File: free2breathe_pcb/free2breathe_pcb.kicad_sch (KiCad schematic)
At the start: 96 parts, among them J1 USB4110-GF-A_REVB, J2 LED_Connector, J3 Alarm_Connector, Q1 AO3401A, Q2 DMN3404L, SW1 Power_Switch, U1 IP5328, U2 MCP6044-E/P, U3 MCP6044-E/P, U4 SO2 Sensor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

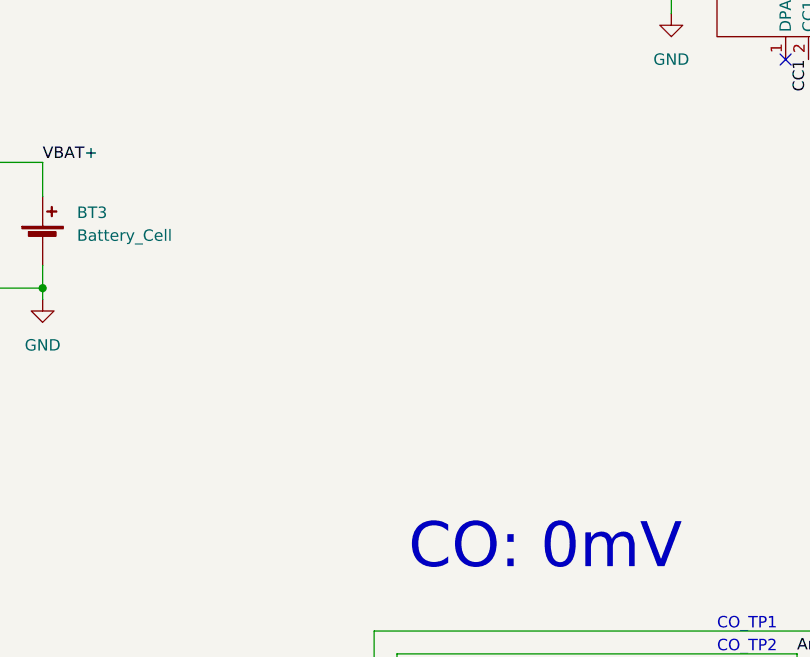
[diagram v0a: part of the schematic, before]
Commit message: initial arrangement for new layout, add mounting holes
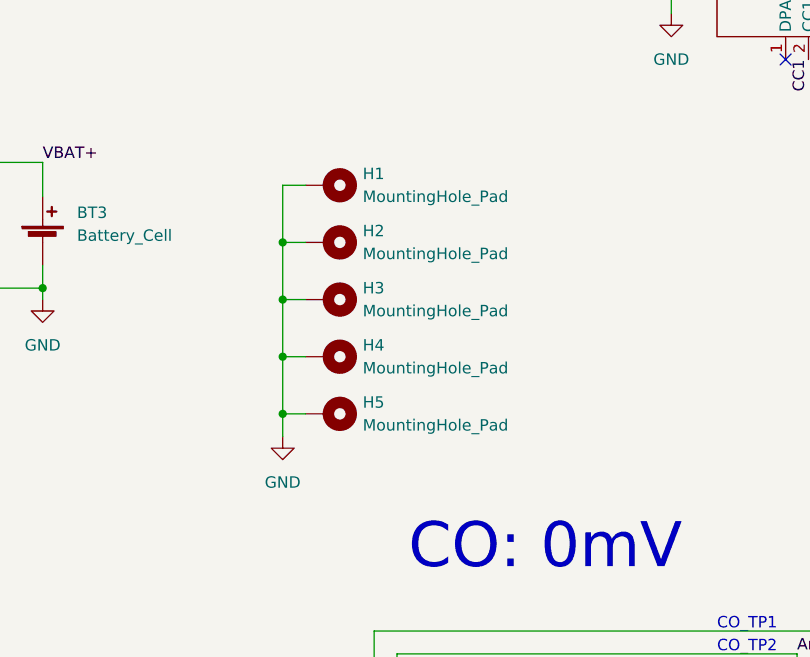
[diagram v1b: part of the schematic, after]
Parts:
- added H1, H2, H3, H4, H5: MountingHole_Pad, MountingHole:MountingHole_3.2mm_M3, symbol Mechanical:MountingHole_Pad
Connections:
- net GND: now also H1.1, H2.1, H3.1, H4.1, H5.1

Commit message: further refinement
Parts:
- J2: footprint Connector_JST:JST_PH_B3B-PH-K_1x03_P2.00mm_Vertical -> Connector_JST:JST_PH_S3B-PH-K_1x03_P2.00mm_Horizontal
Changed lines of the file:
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@@
       (effects (font (size 1.27 1.27)) (justify left))
     )
-    (property "Footprint" "Connector_JST:JST_PH_B3B-PH-K_1x03_P2.00mm_Vertical" (id 2) (at 398.78 88.9 0)
+    (property "Footprint" "Connector_JST:JST_PH_S3B-PH-K_1x03_P2.00mm_Horizontal" (id 2) (at 398.78 88.9 0)
       (effects (font (size 1.27 1.27)) hide)
     )
@@
     )
     (path "/c4414011-bc6e-427d-914d-4b02080af175"
-      (reference "J2") (unit 1) (value "LED_Connector") (footprint "Connector_JST:JST_PH_B3B-PH-K_1x03_P2.00mm_Vertical")
+      (reference "J2") (unit 1) (value "LED_Connector") (footprint "Connector_JST:JST_PH_S3B-PH-K_1x03_P2.00mm_Horizontal")
     )
     (path "/4bd3da1a-b4fb-485a-b13c-20d04d4b9acb"

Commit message: placed components, changed power LEDs
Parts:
- D5, D6, D7, D8: footprint LED_THT:LED_D3.0mm -> LED_SMD:LED_0603_1608Metric
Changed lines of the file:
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@@
     (property "Reference" "D5" (id 0) (at 203.2 118.11 0))
     (property "Value" "LED" (id 1) (at 207.01 121.92 0))
-    (property "Footprint" "LED_THT:LED_D3.0mm" (id 2) (at 203.2 120.65 0)
+    (property "Footprint" "LED_SMD:LED_0603_1608Metric" (id 2) (at 203.2 120.65 0)
       (effects (font (size 1.27 1.27)) hide)
     )
@@
     (property "Reference" "D8" (id 0) (at 193.04 135.89 0))
     (property "Value" "LED" (id 1) (at 196.85 134.62 0))
-    (property "Footprint" "LED_THT:LED_D3.0mm" (id 2) (at 193.04 133.35 0)
+    (property "Footprint" "LED_SMD:LED_0603_1608Metric" (id 2) (at 193.04 133.35 0)
       (effects (font (size 1.27 1.27)) hide)
     )
@@
     (property "Reference" "D7" (id 0) (at 193.04 127 0))
     (property "Value" "LED" (id 1) (at 196.85 130.81 0))
-    (property "Footprint" "LED_THT:LED_D3.0mm" (id 2) (at 193.04 129.54 0)
+    (property "Footprint" "LED_SMD:LED_0603_1608Metric" (id 2) (at 193.04 129.54 0)
       (effects (font (size 1.27 1.27)) hide)
     )
@@
     (property "Reference" "D6" (id 0) (at 200.66 123.19 0))
     (property "Value" "LED" (id 1) (at 203.2 127 0))
-    (property "Footprint" "LED_THT:LED_D3.0mm" (id 2) (at 203.2 124.46 0)
+    (property "Footprint" "LED_SMD:LED_0603_1608Metric" (id 2) (at 203.2 124.46 0)
       (effects (font (size 1.27 1.27)) hide)
     )
@@
     )
     (path "/0299984f-df78-48cc-bdc6-090d3e9cd159"
-      (reference "D5") (unit 1) (value "LED") (footprint "LED_THT:LED_D3.0mm")
+      (reference "D5") (unit 1) (value "LED") (footprint "LED_SMD:LED_0603_1608Metric")
     )
     (path "/b01b1188-32bd-4fd4-b4d9-a13c45d1c9c1"
-      (reference "D6") (unit 1) (value "LED") (footprint "LED_THT:LED_D3.0mm")
+      (reference "D6") (unit 1) (value "LED") (footprint "LED_SMD:LED_0603_1608Metric")
     )
     (path "/5d679726-a4e8-43e7-be42-4533ed656c2e"
-      (reference "D7") (unit 1) (value "LED") (footprint "LED_THT:LED_D3.0mm")
+      (reference "D7") (unit 1) (value "LED") (footprint "LED_SMD:LED_0603_1608Metric")
     )
     (path "/04248967-0a57-4abc-9e67-35cfb5f78fd9"
-      (reference "D8") (unit 1) (value "LED") (footprint "LED_THT:LED_D3.0mm")
+      (reference "D8") (unit 1) (value "LED") (footprint "LED_SMD:LED_0603_1608Metric")
     )
     (path "/3e058933-7aac-40cd-b441-79629738d0a3"

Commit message: more routing
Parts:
- H1, H2, H3, H4, H5: footprint MountingHole:MountingHole_3.2mm_M3 -> MountingHole:MountingHole_3.2mm_M3_Pad_Via
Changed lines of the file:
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@@
       (effects (font (size 1.27 1.27)) (justify left))
     )
-    (property "Footprint" "MountingHole:MountingHole_3.2mm_M3" (id 2) (at 105.41 146.05 0)
+    (property "Footprint" "MountingHole:MountingHole_3.2mm_M3_Pad_Via" (id 2) (at 105.41 146.05 0)
       (effects (font (size 1.27 1.27)) hide)
     )
@@
       (effects (font (size 1.27 1.27)) (justify left))
     )
-    (property "Footprint" "MountingHole:MountingHole_3.2mm_M3" (id 2) (at 105.41 139.7 0)
+    (property "Footprint" "MountingHole:MountingHole_3.2mm_M3_Pad_Via" (id 2) (at 105.41 139.7 0)
       (effects (font (size 1.27 1.27)) hide)
     )
@@
       (effects (font (size 1.27 1.27)) (justify left))
     )
-    (property "Footprint" "MountingHole:MountingHole_3.2mm_M3" (id 2) (at 105.41 152.4 0)
+    (property "Footprint" "MountingHole:MountingHole_3.2mm_M3_Pad_Via" (id 2) (at 105.41 152.4 0)
       (effects (font (size 1.27 1.27)) hide)
     )
@@
       (effects (font (size 1.27 1.27)) (justify left))
     )
-    (property "Footprint" "MountingHole:MountingHole_3.2mm_M3" (id 2) (at 105.41 165.1 0)
+    (property "Footprint" "MountingHole:MountingHole_3.2mm_M3_Pad_Via" (id 2) (at 105.41 165.1 0)
       (effects (font (size 1.27 1.27)) hide)
     )
@@
       (effects (font (size 1.27 1.27)) (justify left))
     )
-    (property "Footprint" "MountingHole:MountingHole_3.2mm_M3" (id 2) (at 105.41 158.75 0)
+    (property "Footprint" "MountingHole:MountingHole_3.2mm_M3_Pad_Via" (id 2) (at 105.41 158.75 0)
       (effects (font (size 1.27 1.27)) hide)
     )
@@
     )
     (path "/3e058933-7aac-40cd-b441-79629738d0a3"
-      (reference "H1") (unit 1) (value "MountingHole_Pad") (footprint "MountingHole:MountingHole_3.2mm_M3")
+      (reference "H1") (unit 1) (value "MountingHole_Pad") (footprint "MountingHole:MountingHole_3.2mm_M3_Pad_Via")
     )
     (path "/3ae0b7cc-c4c5-42a0-ba58-20994b18ddcb"
-      (reference "H2") (unit 1) (value "MountingHole_Pad") (footprint "MountingHole:MountingHole_3.2mm_M3")
+      (reference "H2") (unit 1) (value "MountingHole_Pad") (footprint "MountingHole:MountingHole_3.2mm_M3_Pad_Via")
     )
     (path "/44a4c3b3-90cd-4ca6-b7f3-8c329523b9c4"
-      (reference "H3") (unit 1) (value "MountingHole_Pad") (footprint "MountingHole:MountingHole_3.2mm_M3")
+      (reference "H3") (unit 1) (value "MountingHole_Pad") (footprint "MountingHole:MountingHole_3.2mm_M3_Pad_Via")
     )
     (path "/82e9b2e9-432f-44f2-956a-61a2e063503a"
-      (reference "H4") (unit 1) (value "MountingHole_Pad") (footprint "MountingHole:MountingHole_3.2mm_M3")
+      (reference "H4") (unit 1) (value "MountingHole_Pad") (footprint "MountingHole:MountingHole_3.2mm_M3_Pad_Via")
     )
     (path "/54570a55-2fea-47e6-9d91-f42ccc350ea4"
-      (reference "H5") (unit 1) (value "MountingHole_Pad") (footprint "MountingHole:MountingHole_3.2mm_M3")
+      (reference "H5") (unit 1) (value "MountingHole_Pad") (footprint "MountingHole:MountingHole_3.2mm_M3_Pad_Via")
     )
     (path "/da0efc7a-01ab-44ff-bf6d-4e1e4b0cafb5"

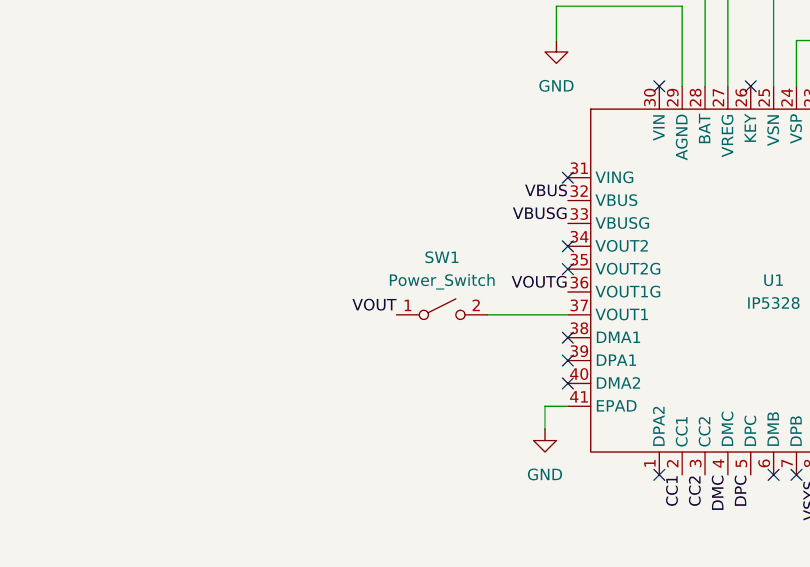
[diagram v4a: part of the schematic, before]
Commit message: add 3d models
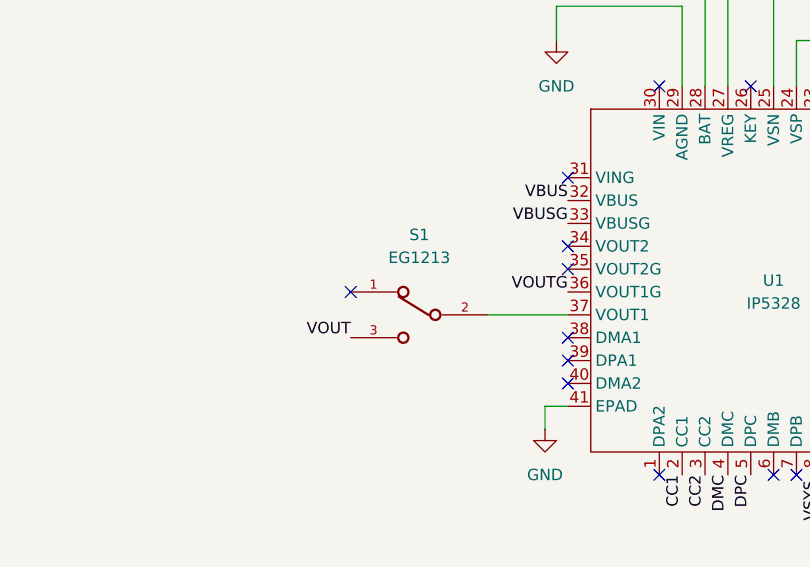
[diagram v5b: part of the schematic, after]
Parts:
- removed SW1: Power_Switch, switch:switch_pad, symbol Switch:SW_SPST
- added S1: EG1213, components:SW_EG1213, symbol EG1213:EG1213
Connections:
- net VOUT: now also S1.3
- net at U1.37 (VOUT1): now also S1.2
- no-connect marks 27 -> 28
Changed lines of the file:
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@@
   (no_connect (at 69.85 53.34))
   (no_connect (at 307.34 85.09))
+  (no_connect (at 121.92 105.41))
   (no_connect (at 171.45 125.73))
   (no_connect (at 34.29 58.42))
@@
     (effects (font (size 1.27 1.27)) (justify right bottom))
   )
-  (label "VOUT" (at 127 107.95 180)
+  (label "VOUT" (at 121.92 110.49 180)
     (effects (font (size 1.27 1.27)) (justify right bottom))
   )
@@
     (pin "2")
   )
+  (symbol (lib_id "EG1213:EG1213") (at 129.54 107.95 0) (unit 1)
+    (in_bom yes) (on_board yes) (fields_autoplaced)
+    (property "Reference" "S1" (id 0) (at 129.54 99.06 0))
+    (property "Value" "EG1213" (id 1) (at 129.54 101.6 0))
+    (property "Footprint" "components:SW_EG1213" (id 2) (at 129.54 107.95 0)
+      (effects (font (size 1.27 1.27)) (justify bottom) hide)
+    )
+    (property "Datasheet" "" (id 3) (at 129.54 107.95 0)
+      (effects (font (size 1.27 1.27)) hide)
+    )
+    (property "MANUFACTURER" "E-Switch" (id 4) (at 129.54 107.95 0)
+      (effects (font (size 1.27 1.27)) (justify bottom) hide)
+    )
+    (pin "1")
+    (pin "2")
+    (pin "3")
+  )
   (symbol (lib_id "power:GND") (at 92.71 309.88 0) (unit 1)
     (in_bom yes) (on_board yes) (fields_autoplaced)
@@
     (pin "2")
   )
-  (symbol (lib_id "Switch:SW_SPST") (at 132.08 107.95 0) (unit 1)
-    (in_bom yes) (on_board yes) (fields_autoplaced)
-    (property "Reference" "SW1" (id 0) (at 132.08 101.6 0))
-    (property "Value" "Power_Switch" (id 1) (at 132.08 104.14 0))
-    (property "Footprint" "switch:switch_pad" (id 2) (at 132.08 107.95 0)
-      (effects (font (size 1.27 1.27)) hide)
-    )
-    (property "Datasheet" "~" (id 3) (at 132.08 107.95 0)
-      (effects (font (size 1.27 1.27)) hide)
-    )
-    (pin "1")
-    (pin "2")
-  )
   (symbol (lib_id "Device:C") (at 212.09 81.28 0) (unit 1)
     (in_bom yes) (on_board yes)
@@
       (reference "R35") (unit 1) (value "10") (footprint "Resistor_SMD:R_0603_1608Metric")
     )
-    (path "/be04bd1f-0a32-47c6-ac53-a5332a5382ed"
-      (reference "SW1") (unit 1) (value "Power_Switch") (footprint "switch:switch_pad")
+    (path "/64b42584-270d-428b-a561-2aaf0f562d08"
+      (reference "S1") (unit 1) (value "EG1213") (footprint "components:SW_EG1213")
     )
     (path "/c9dcc37a-27d4-444a-93cb-b4b7d47a7bbd"

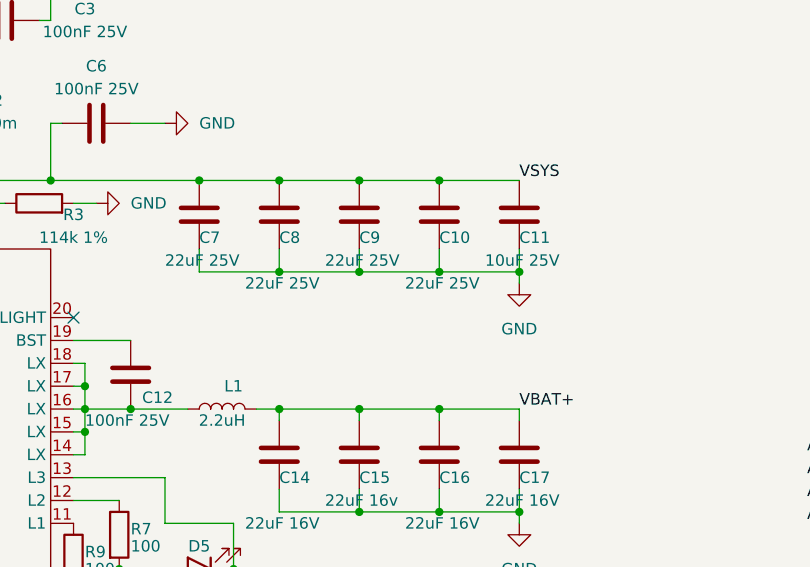
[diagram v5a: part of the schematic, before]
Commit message: update step file to include standard components
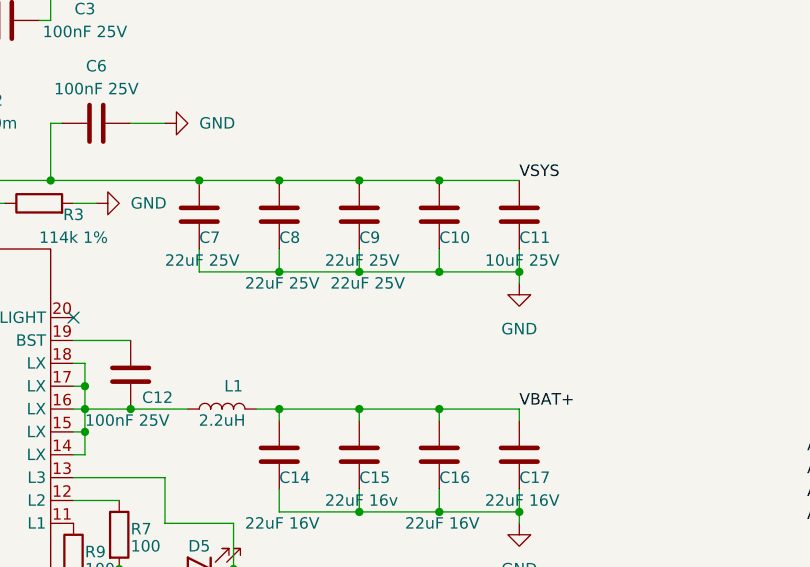
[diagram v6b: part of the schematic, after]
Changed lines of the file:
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@@
     )
     (property "Value" "22uF 25V" (id 1) (at 226.06 88.9 0)
-      (effects (font (size 1.27 1.27)) (justify left))
+      (effects (font (size 1.27 1.27)) (justify right))
     )
     (property "Footprint" "Capacitor_SMD:C_0603_1608Metric" (id 2) (at 230.8352 85.09 0)

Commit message: update components and todo, swap current-sense resistor to 0805
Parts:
- R2: footprint Resistor_SMD:R_0603_1608Metric -> Resistor_SMD:R_0805_2012Metric
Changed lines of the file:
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@@
   (no_connect (at 146.05 110.49))
   (no_connect (at 281.94 90.17))
+  (no_connect (at 166.37 82.55))
   (no_connect (at 281.94 87.63))
   (no_connect (at 146.05 92.71))
   (no_connect (at 146.05 115.57))
-  (no_connect (at 166.37 82.55))
   (no_connect (at 146.05 102.87))
   (no_connect (at 307.34 92.71))
@@
       (effects (font (size 1.27 1.27)) (justify left))
     )
-    (property "Footprint" "Resistor_SMD:R_0603_1608Metric" (id 2) (at 174.752 69.85 90)
+    (property "Footprint" "Resistor_SMD:R_0805_2012Metric" (id 2) (at 174.752 69.85 90)
       (effects (font (size 1.27 1.27)) hide)
     )
@@
     )
     (path "/aac64d76-0462-479d-882d-a1e685ec1bb8"
-      (reference "R2") (unit 1) (value "10m") (footprint "Resistor_SMD:R_0603_1608Metric")
+      (reference "R2") (unit 1) (value "10m") (footprint "Resistor_SMD:R_0805_2012Metric")
     )
     (path "/15f99abf-d997-4083-af3a-6835a9c72472"

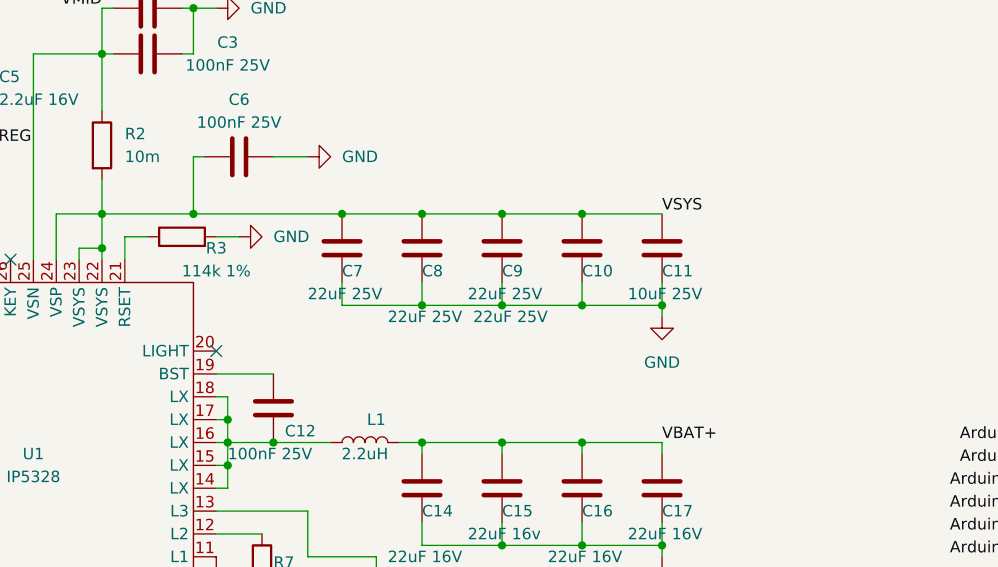
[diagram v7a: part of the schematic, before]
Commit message: add BOM, update board with component replacements
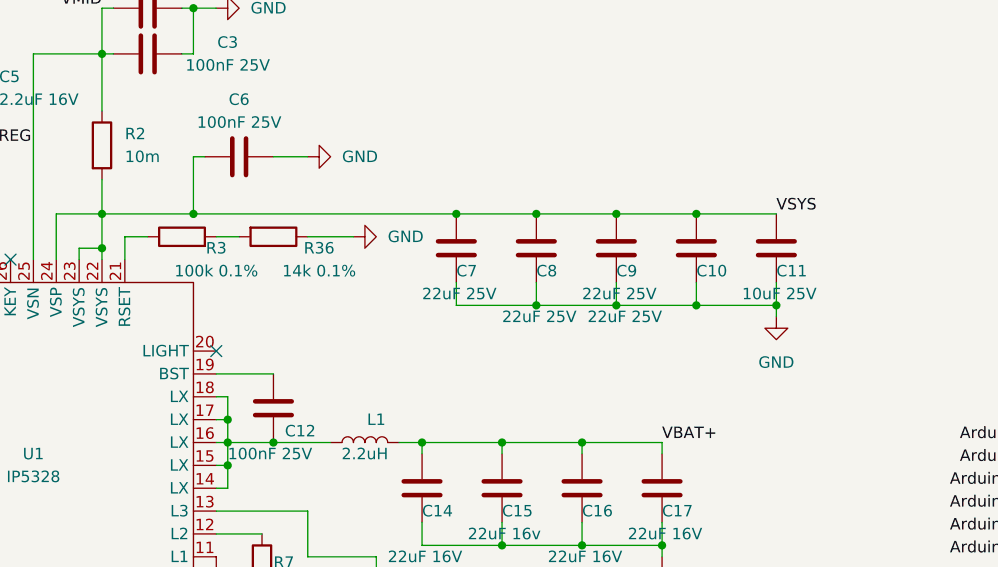
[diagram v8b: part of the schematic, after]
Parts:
- added R36: 14k 0.1%, Resistor_SMD:R_0603_1608Metric, symbol Device:R
- C10, C2, C7, C8, C9: footprint Capacitor_SMD:C_0603_1608Metric -> Capacitor_SMD:C_0805_2012Metric
- R3: value 114k 1% -> 100k 0.1%
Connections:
- net GND: now also R36.1; no longer R3.2
- new net: R3.2, R36.2
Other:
- moved on the sheet: C10, C11, C7, C8, C9
